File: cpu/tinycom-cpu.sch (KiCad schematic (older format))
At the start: 7 parts, among them P1 CONN_02X08, P2 CONN_02X08, U1 OLIMEX_IC_A13, U2 H5TQ2G83BFR/FBGA82, Y1 Crystal

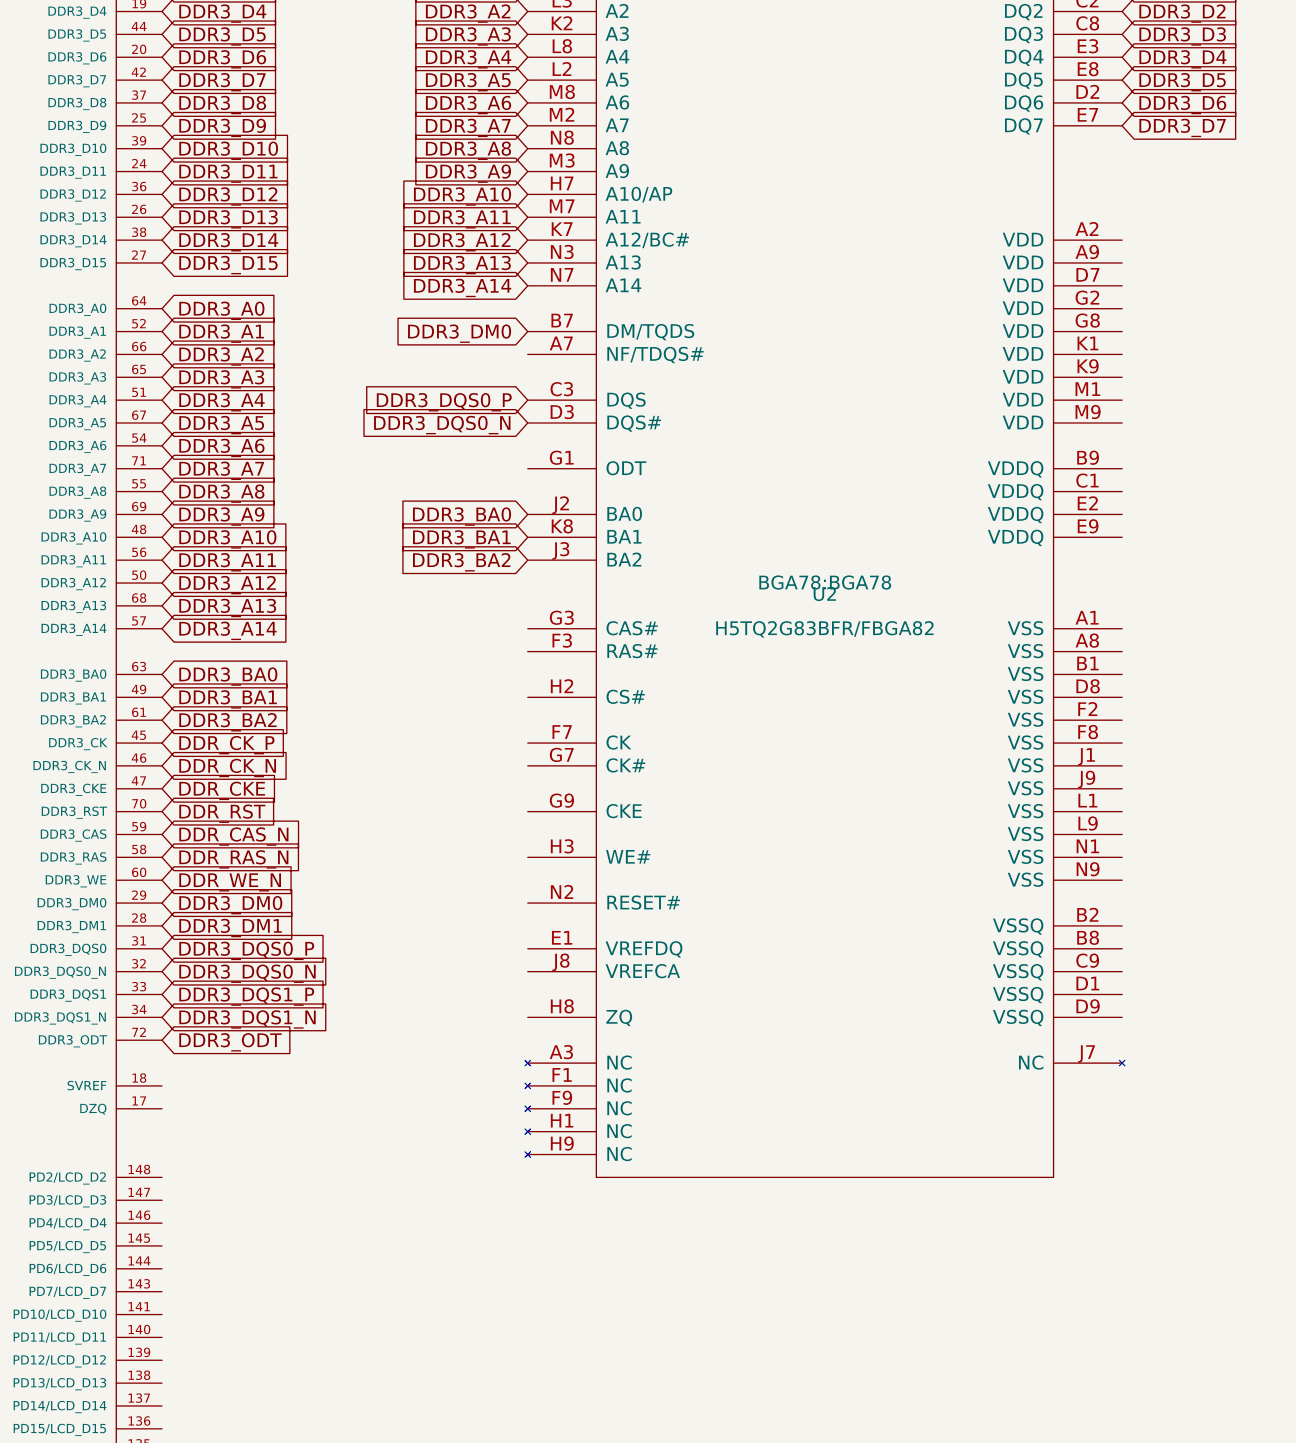
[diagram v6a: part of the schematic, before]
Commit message: route new ddr
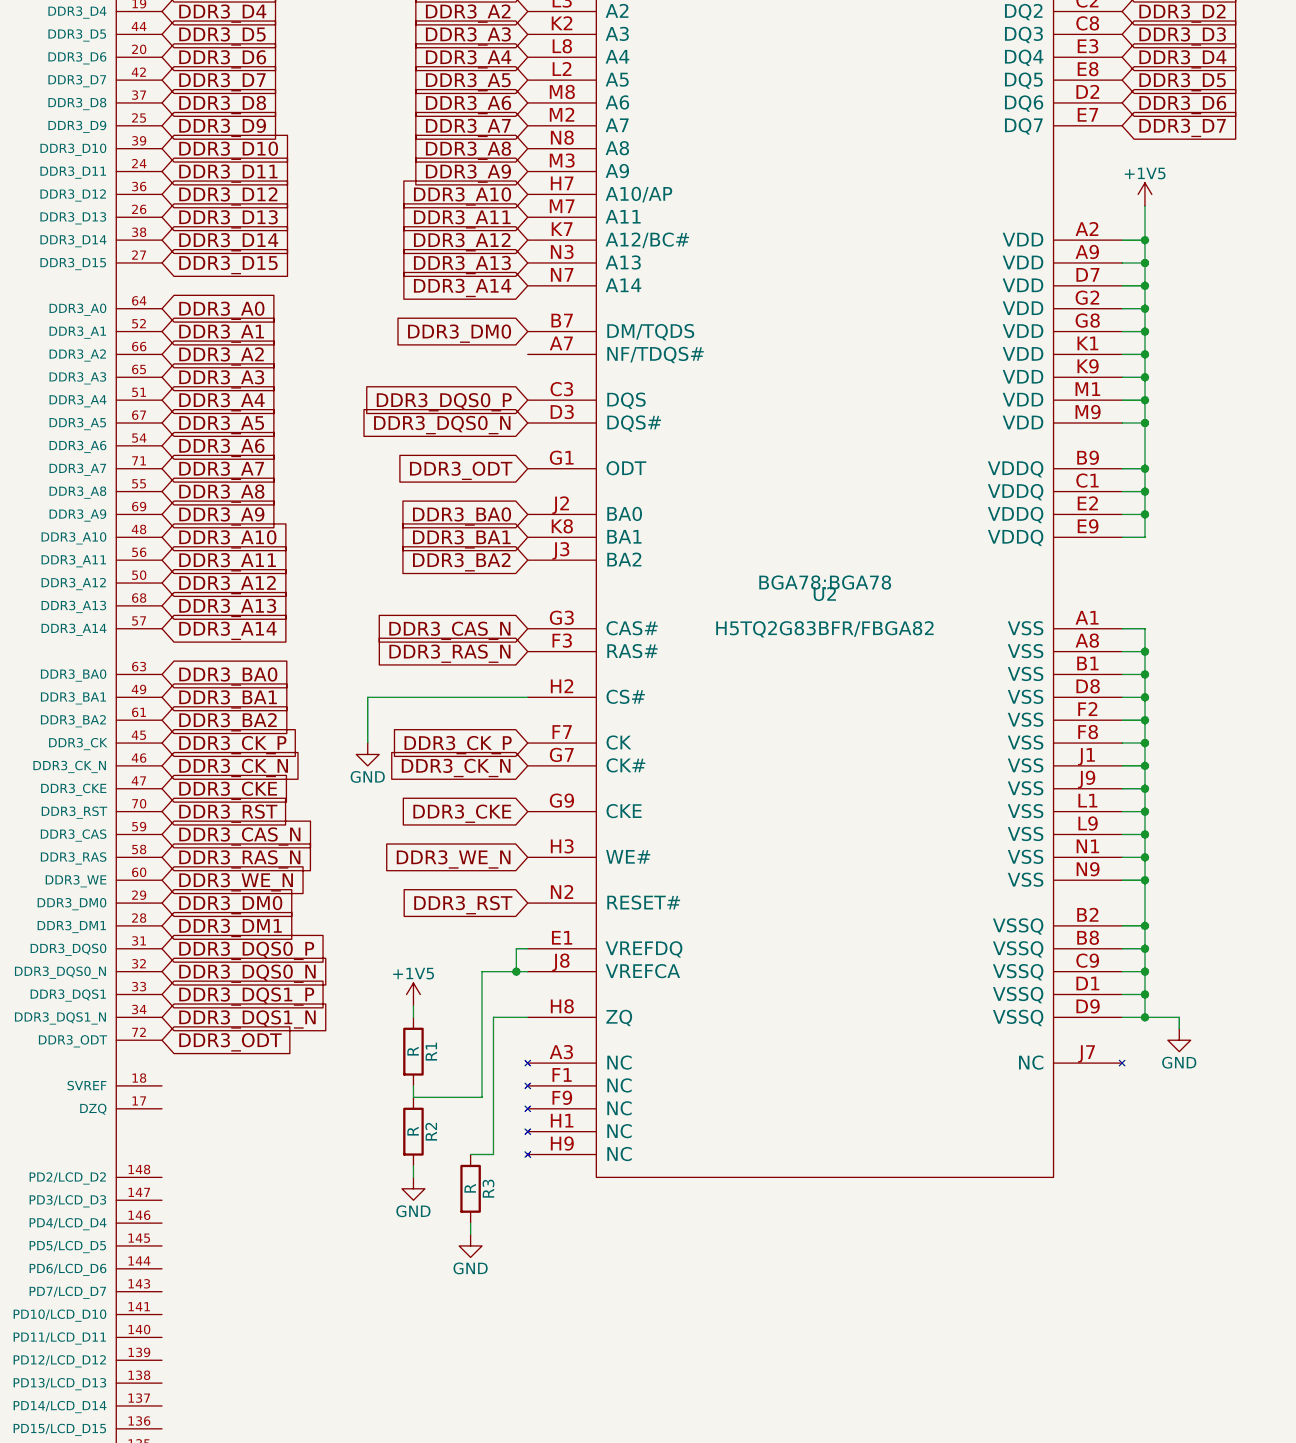
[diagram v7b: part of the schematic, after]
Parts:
- added R1, R2, R3: R, Resistors_SMD:R_0603, symbol R
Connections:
- net DDR_CAS_N is gone; now on net DDR3_CAS_N: U1.59 (DDR3_CAS)
- net DDR_CKE is gone; now on net DDR3_CKE: U1.47 (DDR3_CKE)
- net DDR_CK_N is gone; now on net DDR3_CK_N: U1.46 (DDR3_CK_N)
- net DDR_CK_P is gone; now on net DDR3_CK_P: U1.45 (DDR3_CK)
- net DDR_RAS_N is gone; now on net DDR3_RAS_N: U1.58 (DDR3_RAS)
- net DDR_RST is gone; now on net DDR3_RST: U1.70 (DDR3_RST)
- net DDR_WE_N is gone; now on net DDR3_WE_N: U1.60 (DDR3_WE)
- net +1V5: now also U2.A2 (VDD), U2.A9 (VDD), U2.B9 (VDDQ), U2.C1 (VDDQ), U2.D7 (VDD), U2.E2 (VDDQ), U2.E9 (VDDQ), U2.G2 (VDD), U2.G8 (VDD), U2.K1 (VDD), U2.K9 (VDD), U2.M1 (VDD), U2.M9 (VDD), R1.1
- net DDR3_ODT: now also U2.G1 (ODT)
- net GND: now also U2.A1 (VSS), U2.A8 (VSS), U2.B1 (VSS), U2.B2 (VSSQ), U2.B8 (VSSQ), U2.C9 (VSSQ), U2.D1 (VSSQ), U2.D8 (VSS), U2.D9 (VSSQ), U2.F2 (VSS), U2.F8 (VSS), U2.H2 (CS#), U2.J1 (VSS), U2.J9 (VSS), U2.L1 (VSS), U2.L9 (VSS), U2.N1 (VSS), U2.N9 (VSS), R2.2, R3.2
- net at U2.E1 (VREFDQ): now also U2.J8 (VREFCA), R1.2, R2.1
- net DDR3_RAS_N: now reaches U2.F3 (RAS#)
- net DDR3_CK_P: now reaches U2.F7 (CK)
- net DDR3_CAS_N: now reaches U2.G3 (CAS#)
- net DDR3_CK_N: now reaches U2.G7 (CK#)
- net DDR3_CKE: now reaches U2.G9 (CKE)
- net DDR3_WE_N: now reaches U2.H3 (WE#)
- net at U2.H8 (ZQ): now also R3.1
- net DDR3_RST: now reaches U2.N2 (RESET#)

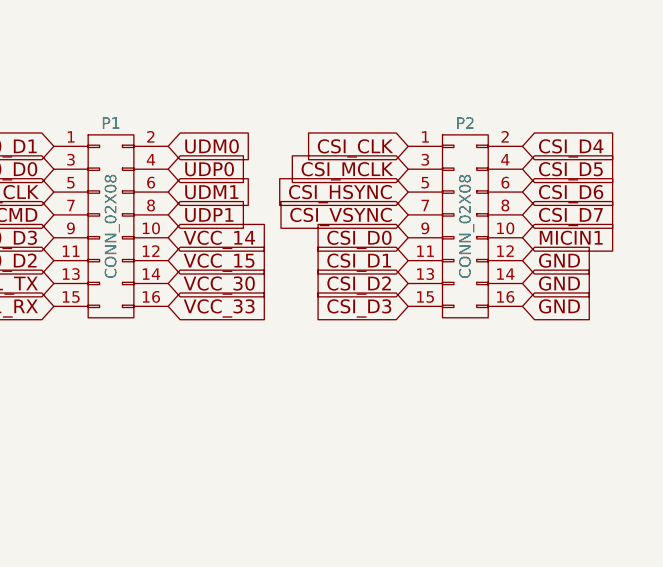
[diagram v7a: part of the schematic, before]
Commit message: add ddr power plane
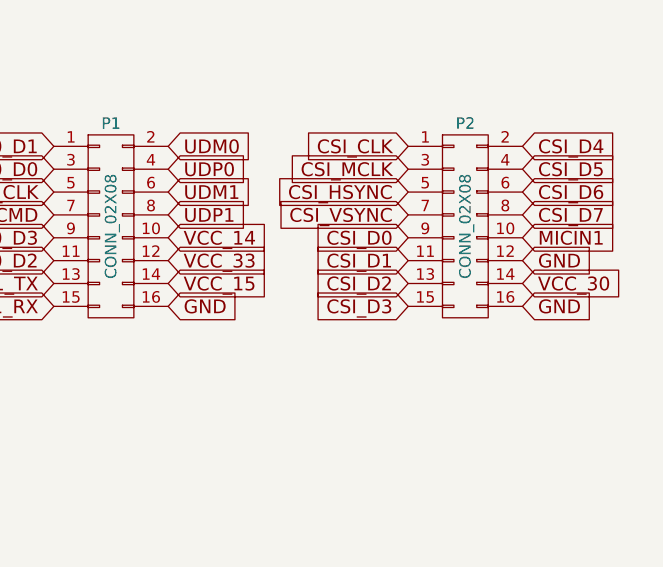
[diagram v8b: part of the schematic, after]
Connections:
- net +1V5: now also P1.14 (P14); no longer P1.12 (P12)
- net +3V3: now also P1.12 (P12); no longer P1.16 (P16)
- net GND: now also P1.16 (P16); no longer P2.14 (P14)
- net VCC_30: now also P2.14 (P14); no longer P1.14 (P14)
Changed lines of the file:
@@
 GND
 Text GLabel 7850 6100 2    60   Input ~ 0
+GND
+Text GLabel 7850 6000 2    60   Input ~ 0
+VCC_15
+Text GLabel 7850 5900 2    60   Input ~ 0
 VCC_33
-Text GLabel 7850 6000 2    60   Input ~ 0
-VCC_30
-Text GLabel 7850 5900 2    60   Input ~ 0
-VCC_15
 Text GLabel 7850 5800 2    60   Input ~ 0
 VCC_14
 Text GLabel 9400 6000 2    60   Input ~ 0
-GND
+VCC_30
 Text GLabel 9400 5900 2    60   Input ~ 0
 GND
